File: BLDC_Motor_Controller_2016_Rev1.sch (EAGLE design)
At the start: 103 parts, among them J3 APP_2POS_CONFIG5V_HORIZ, Q1 MOSFET-NCHANNELFQP30N06L, Q2 MOSFET-NCHANNELFQP30N06L, Q3 MOSFET-NCHANNELFQP30N06L, Q4 MOSFET-NCHANNELFQP30N06L, Q5 MOSFET-NCHANNELFQP30N06L, Q6 MOSFET-NCHANNELFQP30N06L, Q7 MOSFET-PCHANNEL, Q8 MOSFET-PCHANNEL

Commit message: Fixed first board review issues
- FET for PVDD LED
- Widened input voltage polygon
- Added 15V zener on FET gates
- Added test points
- Added pull ups on hall-effect lines
- Added filter on PWM input
- Changed voltage divider resistor values
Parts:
- added 1M, 3M: 330, SparkFun-Passives:RESISTOR0805-RES
- added C40: .015u, SparkFun-Passives:CAP0805
- added D10, D11, D12, D13, D14, D15: 3.3V, SparkFun-DiscreteSemi:DIODE-ZENER3.3V
- added Q9: MOSFET-NCHANNELAO3404A, SparkFun-DiscreteSemi:MOSFET-NCHANNELAO3404A
- added R31: 100, SparkFun-Passives:RESISTOR0805-RES
- added R36, R37, R38: 10k, SparkFun-Passives:RESISTOR0805-RES
- added U$10, U$11, U$12, U$15, U$16, U$17, U$18, U$19, U$20, U$21, U$22, U$23, U$24, U$25: TEST_POINT_0.1INDIAM, MRDT-Connectors:TEST_POINT_0.1INDIAM
- R14, R19, R24, R26: value 34.8k -> 46.4k
- R32: value 1k -> 330; device SparkFun-Passives:RESISTOR1206 -> SparkFun-Passives:RESISTOR0805-RES
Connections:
- new net N$37: R31.2, U$4.4
- new net N$38: 1M.1, 3M.2, Q9.G
- new net N$41: D6.A, Q9.S
- new net N$42: U$20.P$1
- new net N$43: U$21.P$1
- new net N$44: U$22.P$1
- new net N$45: U$23.P$1
- new net N$46: U$24.P$1
- new net N$47: U$25.P$1
- net GH_A: now also U$17.P$1
- net GH_B: now also U$19.P$1
- net GL_A: now also U$18.P$1
- net GND: now also 1M.2, C40.2, D15.A
- net N$13: now also D13.C
- net N$14: now also D11.C
- net N$15: now also D10.C
- net N$16: now also D12.C
- net N$17: now also D14.C
- net N$18: now also D15.C
- net N$20: now also R36.2
- net N$33: now also R38.2
- net N$39: now also R37.2
- net PVDD: now also 3M.1, U$10.P$1; no longer D6.A
- net SH_A: now also D13.A, U$12.P$1
- net SH_B: now also D11.A, U$15.P$1
- net SH_C: now also D14.A, U$16.P$1
- net SL_A: now also D12.A
- net SL_B: now also D10.A
- net SPEED_IN: now also C40.1, R31.1; no longer U$4.4
- net VCC: now also Q9.D, R36.1, R37.1, R38.1, U$11.P$1
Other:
- moved on the sheet: D6, R32

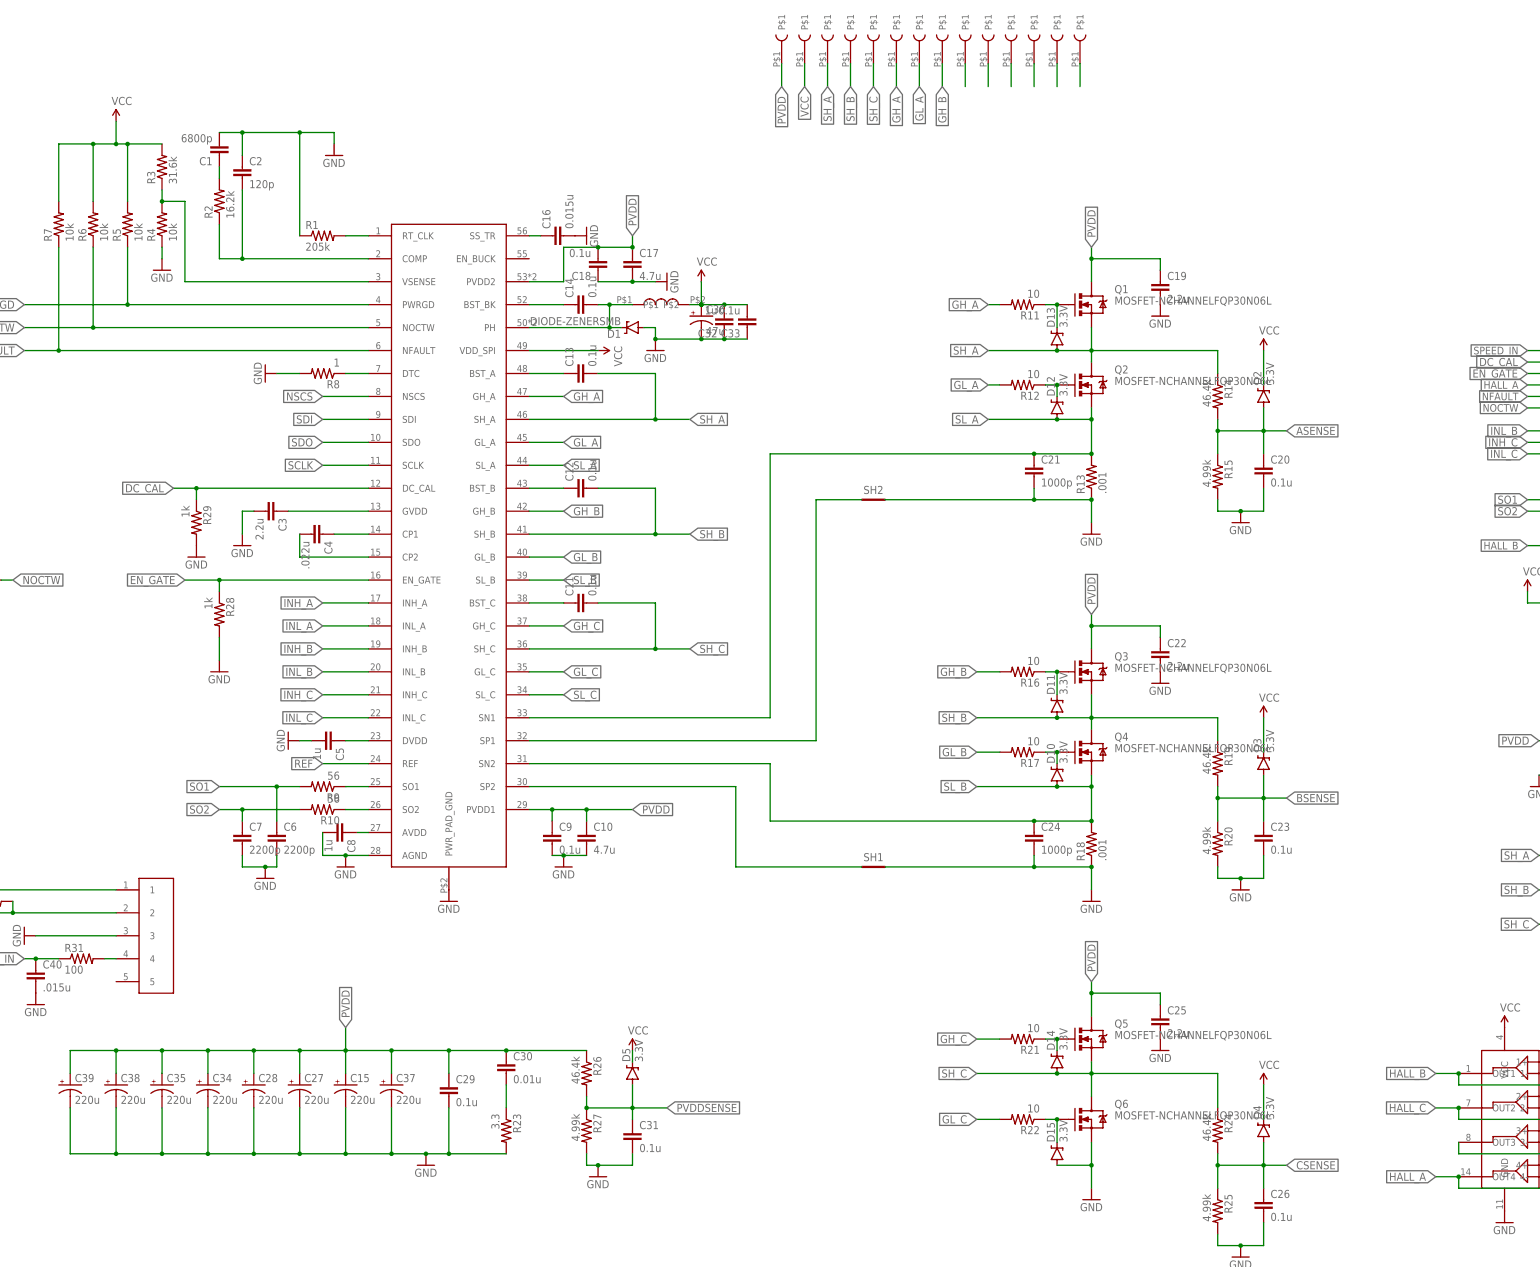
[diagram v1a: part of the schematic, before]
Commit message: Routed test points
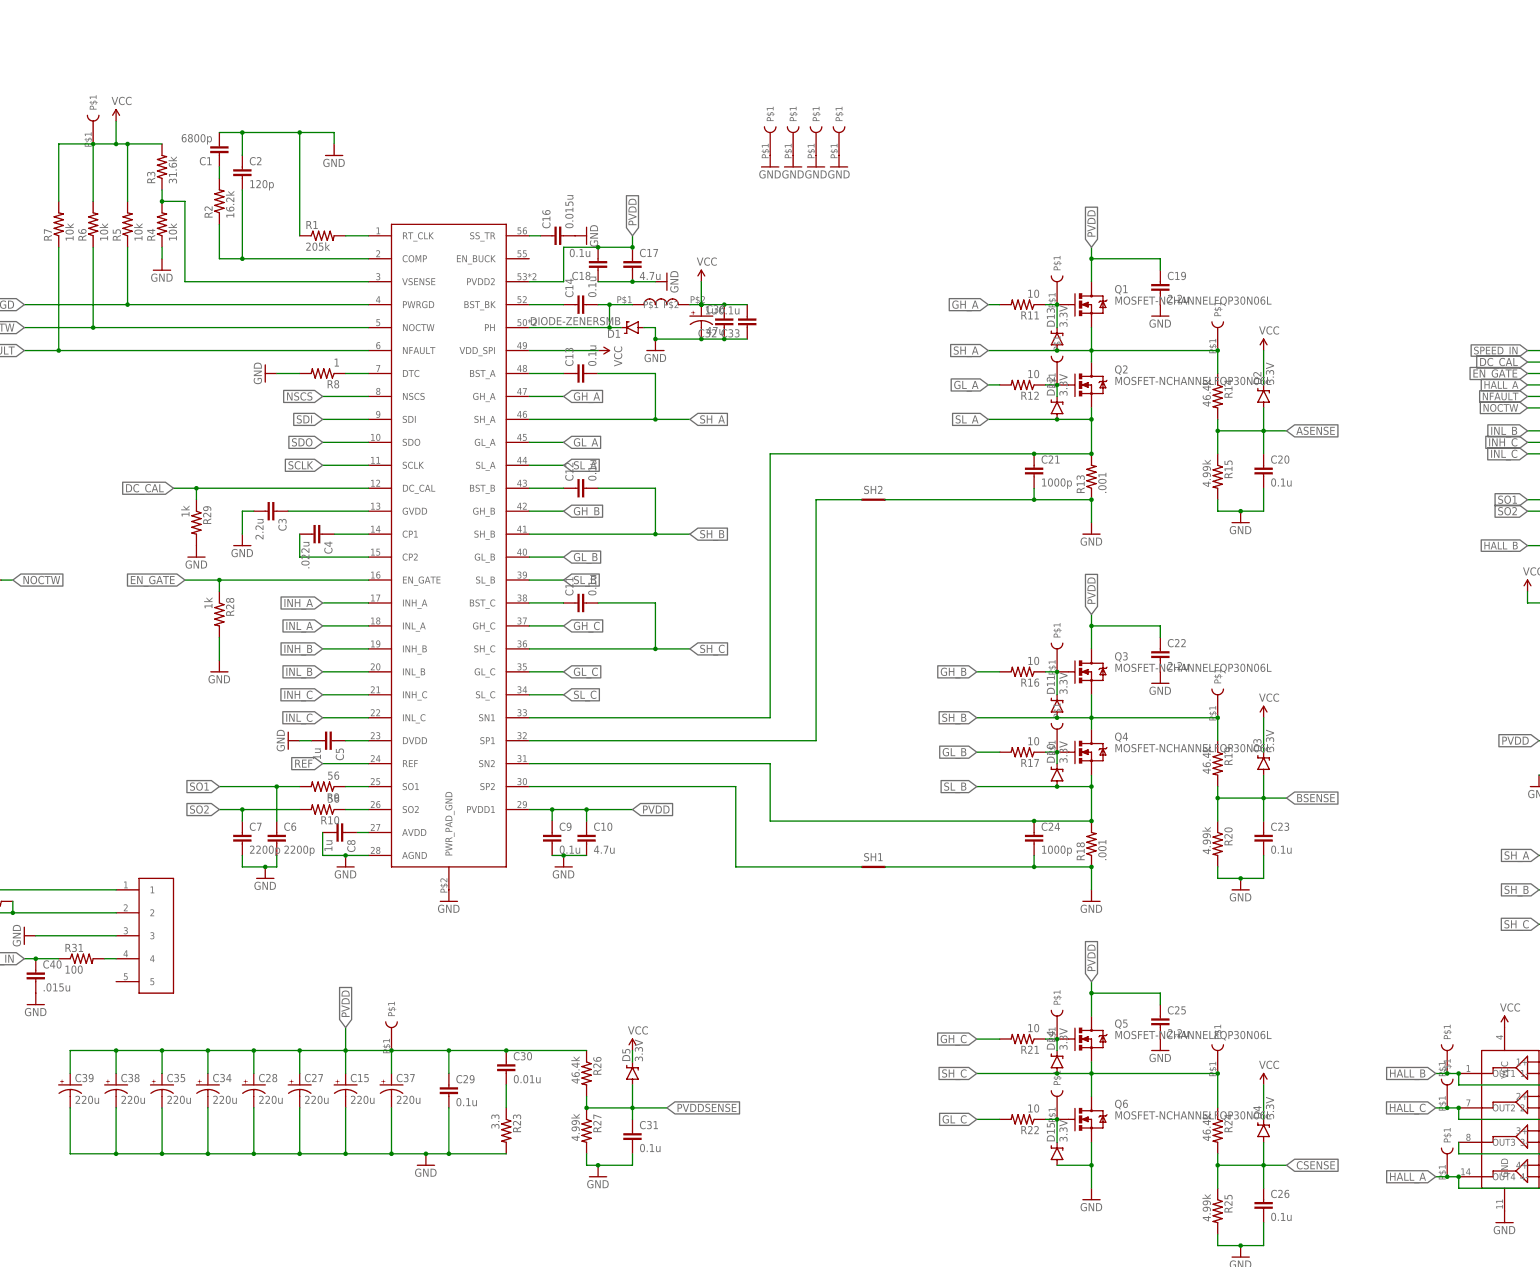
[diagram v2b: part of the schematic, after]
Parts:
- added U$26, U$27, U$28, U$29: TEST_POINT_0.1INDIAM, MRDT-Connectors:TEST_POINT_0.1INDIAM
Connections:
- removed net N$42: U$20.P$1
- removed net N$43: U$21.P$1
- removed net N$44: U$22.P$1
- removed net N$45: U$23.P$1
- removed net N$46: U$24.P$1
- removed net N$47: U$25.P$1
- net GH_A: no longer U$17.P$1
- net GH_B: no longer U$19.P$1
- net GL_A: no longer U$18.P$1
- net GND: now also U$26.P$1, U$27.P$1, U$28.P$1, U$29.P$1
- net HALL_A: now also U$23.P$1
- net HALL_B: now also U$21.P$1
- net HALL_C: now also U$22.P$1
- net N$13: now also U$12.P$1
- net N$14: now also U$16.P$1
- net N$15: now also U$17.P$1
- net N$16: now also U$15.P$1
- net N$17: now also U$18.P$1
- net N$18: now also U$19.P$1
- net PVDD: now also U$11.P$1; no longer U$10.P$1
- net SH_A: now also U$25.P$1; no longer U$12.P$1
- net SH_B: now also U$24.P$1; no longer U$15.P$1
- net SH_C: now also U$20.P$1; no longer U$16.P$1
- net VCC: now also U$10.P$1; no longer U$11.P$1

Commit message: Fixed board review #2 issues
- Increased polygon isolation
- Removed hall effect buffer and added RC filters on hall effect lines
- Added ground vias around driver backplate
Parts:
- removed U$13: OPAMP_14SOIC, OpAmp_14SOIC:OPAMP_14SOIC
- added C41, C42, C43: .015u, SparkFun-Passives:CAP0805
- added D16: 3.3V, SparkFun-DiscreteSemi:DIODE-ZENER3.3V
- added R39, R40, R41: 10, SparkFun-Passives:RESISTOR0805-RES
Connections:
- removed net N$40: U$13.3-, U$13.OUT3
- net GND: now also C41.2, C42.2, C43.2; no longer U$13.GND
- net HALL_A: now also C41.1, R41.1, U$22.P$1; no longer U$13.4-, U$13.OUT4, U$23.P$1
- net HALL_B: now also C42.1, R40.1; no longer U$13.1-, U$13.OUT1
- net HALL_C: now also C43.1, R39.1, U$23.P$1; no longer U$13.2-, U$13.OUT2, U$22.P$1
- net N$20: now also R37.2, R39.2, U$8.2; no longer R36.2, U$13.1+, U$8.3
- net N$33: now also R36.2, R40.2, U$8.3; no longer R38.2, U$13.4+, U$8.4
- net N$38: now also D16.C
- net N$39: now also R38.2, R41.2, U$8.4; no longer R37.2, U$13.2+, U$8.2
- net N$41: now also D16.A
- net VCC: no longer U$13.VCC
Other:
- moved on the sheet: 1M, R36, R37, R38

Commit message: MAX3077 was back on board for some reason, reswitched to MAX7078
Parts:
- removed U$3: MAX3077, MRDT-2015-General:MAX3077
- added U$13: MAX3078E, MRDT-ICs:MAX3078E
- R50: value 330 -> 3M
- R51: value 330 -> 1M
- renumbered 1M to R51, 3M to R50
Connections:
- new net DE: U$13.DE, U$2.PC7
- new net NRE: U$13.NRE, U$2.PD6
- net GND: now also U$13.GND; no longer U$3.GND
- net N$34: now also U$13.A; no longer U$3.B, U$3.Z
- net N$36: now also U$13.B; no longer U$3.A, U$3.Y
- net RX: now also U$13.RO; no longer U$3.RO
- net TX: now also U$13.DI; no longer U$3.DI
- net VCC: now also U$13.VCC; no longer U$3.VCC
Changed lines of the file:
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@@
 <?xml version="1.0" encoding="utf-8"?>
 <!DOCTYPE eagle SYSTEM "eagle.dtd">
-<eagle version="7.3.0">
+<eagle version="7.4.0">
 <drawing>
 <settings>
@@
 <part name="J3" library="MRDT-Connectors" deviceset="APP_2POS_CONFIG" device="5V_HORIZ"/>
 <part name="C38" library="SparkFun-Passives" deviceset="CAP_POL" device="PTH4" value="220u"/>
-<part name="U$3" library="MRDT-2015-General" deviceset="MAX3077" device=""/>
 <part name="R30" library="SparkFun-Passives" deviceset="RESISTOR" device="0805-RES" value="120"/>
 <part name="U$4" library="Molex-SL" deviceset="5PIN" device=""/>
@@
 <part name="R38" library="SparkFun-Passives" deviceset="RESISTOR" device="0805-RES" value="10k"/>
 <part name="Q9" library="SparkFun-DiscreteSemi" deviceset="MOSFET-NCHANNEL" device="AO3404A"/>
-<part name="1M" library="SparkFun-Passives" deviceset="RESISTOR" device="0805-RES" value="330"/>
-<part name="3M" library="SparkFun-Passives" deviceset="RESISTOR" device="0805-RES" value="330"/>
+<part name="R51" library="SparkFun-Passives" deviceset="RESISTOR" device="0805-RES" value="1M"/>
+<part name="R50" library="SparkFun-Passives" deviceset="RESISTOR" device="0805-RES" value="3M"/>
 <part name="GND35" library="SparkFun-Aesthetics" deviceset="GND" device=""/>
 <part name="D10" library="SparkFun-DiscreteSemi" deviceset="DIODE-ZENER" device="3.3V" value="3.3V"/>
@@
 <part name="GND33" library="SparkFun-Aesthetics" deviceset="GND" device=""/>
 <part name="D16" library="SparkFun-DiscreteSemi" deviceset="DIODE-ZENER" device="3.3V" value="3.3V"/>
+<part name="U$13" library="MRDT-ICs" deviceset="MAX3078E" device=""/>
 </parts>
 <sheets>
@@
 <instance part="J3" gate="VCC" x="256.54" y="-45.72"/>
 <instance part="C38" gate="G$1" x="-73.66" y="-121.92"/>
-<instance part="U$3" gate="G$1" x="-121.92" y="-96.52"/>
 <instance part="R30" gate="G$1" x="-101.6" y="-81.28"/>
 <instance part="U$4" gate="G$1" x="-66.04" y="-91.44"/>
 <instance part="GND36" gate="1" x="-93.98" y="-88.9" rot="R270"/>
-<instance part="GND37" gate="1" x="-147.32" y="-101.6"/>
+<instance part="GND37" gate="1" x="-116.84" y="-93.98"/>
 <instance part="C39" gate="G$1" x="-83.82" y="-121.92"/>
 <instance part="SH1" gate="G$1" x="93.98" y="-73.66"/>
@@
 <instance part="R38" gate="G$1" x="261.62" y="-116.84" rot="R270"/>
 <instance part="Q9" gate="G$1" x="-165.1" y="-12.7"/>
-<instance part="1M" gate="G$1" x="-177.8" y="-20.32" rot="R270"/>
-<instance part="3M" gate="G$1" x="-182.88" y="-12.7"/>
+<instance part="R51" gate="G$1" x="-177.8" y="-20.32" rot="R270"/>
+<instance part="R50" gate="G$1" x="-182.88" y="-12.7"/>
 <instance part="GND35" gate="1" x="-177.8" y="-30.48"/>
 <instance part="D10" gate="G$1" x="134.62" y="-53.34" rot="R90"/>
@@
 <instance part="GND33" gate="1" x="241.3" y="-154.94"/>
 <instance part="D16" gate="G$1" x="-172.72" y="-17.78" rot="R90"/>
+<instance part="U$13" gate="G$1" x="-127" y="-81.28"/>
 </instances>
 <busses>
@@
 </segment>
 <segment>
-<pinref part="U$3" gate="G$1" pin="GND"/>
-<pinref part="GND37" gate="1" pin="GND"/>
-<wire x1="-144.78" y1="-93.98" x2="-147.32" y2="-93.98" width="0.1524" layer="91"/>
-<wire x1="-147.32" y1="-93.98" x2="-147.32" y2="-99.06" width="0.1524" layer="91"/>
-</segment>
-<segment>
 <pinref part="U$4" gate="G$1" pin="3"/>
 <pinref part="GND36" gate="1" pin="GND"/>
@@
 </segment>
 <segment>
-<pinref part="1M" gate="G$1" pin="2"/>
+<pinref part="R51" gate="G$1" pin="2"/>
 <pinref part="GND35" gate="1" pin="GND"/>
 <wire x1="-177.8" y1="-27.94" x2="-177.8" y2="-25.4" width="0.1524" layer="91"/>
@@
 <pinref part="C42" gate="G$1" pin="2"/>
 <wire x1="241.3" y1="-149.86" x2="241.3" y2="-152.4" width="0.1524" layer="91"/>
+</segment>
+<segment>
+<pinref part="U$13" gate="G$1" pin="GND"/>
+<pinref part="GND37" gate="1" pin="GND"/>
+<wire x1="-116.84" y1="-91.44" x2="-116.84" y2="-88.9" width="0.1524" layer="91"/>
 </segment>
 </net>
@@
 </segment>
 <segment>
-<pinref part="U$3" gate="G$1" pin="VCC"/>
-<wire x1="-144.78" y1="-78.74" x2="-147.32" y2="-78.74" width="0.1524" layer="91"/>
-<wire x1="-147.32" y1="-78.74" x2="-147.32" y2="-73.66" width="0.1524" layer="91"/>
-<label x="-147.32" y="-73.66" size="1.778" layer="95" rot="R90" xref="yes"/>
+<wire x1="-116.84" y1="-73.66" x2="-116.84" y2="-71.12" width="0.1524" layer="91"/>
+<label x="-116.84" y="-71.12" size="1.778" layer="95" rot="R90" xref="yes"/>
+<pinref part="U$13" gate="G$1" pin="VCC"/>
 </segment>
 <segment>
@@
 </segment>
 <segment>
-<pinref part="3M" gate="G$1" pin="1"/>
+<pinref part="R50" gate="G$1" pin="1"/>
 <wire x1="-187.96" y1="-5.08" x2="-187.96" y2="-12.7" width="0.1524" layer="91"/>
 <label x="-187.96" y="-5.08" size="1.778" layer="95" rot="R90" xref="yes"/>
@@
 </segment>
 <segment>
-<pinref part="U$3" gate="G$1" pin="DI"/>
-<wire x1="-144.78" y1="-88.9" x2="-147.32" y2="-88.9" width="0.1524" layer="91"/>
-<label x="-147.32" y="-88.9" size="1.778" layer="95" rot="R180" xref="yes"/>
+<wire x1="-139.7" y1="-88.9" x2="-144.78" y2="-88.9" width="0.1524" layer="91"/>
+<label x="-144.78" y="-88.9" size="1.778" layer="95" rot="R180" xref="yes"/>
+<pinref part="U$13" gate="G$1" pin="DI"/>
 </segment>
 </net>
@@
 </segment>
 <segment>
-<pinref part="U$3" gate="G$1" pin="RO"/>
-<wire x1="-144.78" y1="-83.82" x2="-147.32" y2="-83.82" width="0.1524" layer="91"/>
-<label x="-147.32" y="-83.82" size="1.778" layer="95" rot="R180" xref="yes"/>
+<wire x1="-139.7" y1="-73.66" x2="-144.78" y2="-73.66" width="0.1524" layer="91"/>
+<label x="-144.78" y="-73.66" size="1.778" layer="95" rot="R180" xref="yes"/>
+<pinref part="U$13" gate="G$1" pin="RO"/>
 </segment>
 </net>
@@
 <net name="N$34" class="0">
 <segment>
-<pinref part="U$3" gate="G$1" pin="B"/>
-<pinref part="U$3" gate="G$1" pin="Z"/>
-<wire x1="-116.84" y1="-83.82" x2="-116.84" y2="-88.9" width="0.1524" layer="91"/>
 <pinref part="U$4" gate="G$1" pin="2"/>
 <wire x1="-116.84" y1="-83.82" x2="-96.52" y2="-83.82" width="0.1524" layer="91"/>
-<junction x="-116.84" y="-83.82"/>
 <pinref part="R30" gate="G$1" pin="2"/>
 <wire x1="-96.52" y1="-83.82" x2="-73.66" y2="-83.82" width="0.1524" layer="91"/>
 <wire x1="-96.52" y1="-81.28" x2="-96.52" y2="-83.82" width="0.1524" layer="91"/>
 <junction x="-96.52" y="-83.82"/>
+<pinref part="U$13" gate="G$1" pin="A"/>
 </segment>
 </net>
 <net name="N$36" class="0">
 <segment>
-<pinref part="U$3" gate="G$1" pin="A"/>
-<wire x1="-116.84" y1="-78.74" x2="-114.3" y2="-78.74" width="0.1524" layer="91"/>
-<wire x1="-114.3" y1="-78.74" x2="-114.3" y2="-93.98" width="0.1524" layer="91"/>
-<pinref part="U$3" gate="G$1" pin="Y"/>
-<wire x1="-114.3" y1="-93.98" x2="-116.84" y2="-93.98" width="0.1524" layer="91"/>
 <pinref part="U$4" gate="G$1" pin="1"/>
-<wire x1="-114.3" y1="-78.74" x2="-106.68" y2="-78.74" width="0.1524" layer="91"/>
-<junction x="-114.3" y="-78.74"/>
+<wire x1="-116.84" y1="-78.74" x2="-106.68" y2="-78.74" width="0.1524" layer="91"/>
 <pinref part="R30" gate="G$1" pin="1"/>
 <wire x1="-106.68" y1="-78.74" x2="-73.66" y2="-78.74" width="0.1524" layer="91"/>
 <wire x1="-106.68" y1="-81.28" x2="-106.68" y2="-78.74" width="0.1524" layer="91"/>
 <junction x="-106.68" y="-78.74"/>
+<pinref part="U$13" gate="G$1" pin="B"/>
 </segment>
 </net>
@@
 <segment>
 <pinref part="Q9" gate="G$1" pin="G"/>
-<pinref part="3M" gate="G$1" pin="2"/>
+<pinref part="R50" gate="G$1" pin="2"/>
 <wire x1="-172.72" y1="-12.7" x2="-177.8" y2="-12.7" width="0.1524" layer="91"/>
-<pinref part="1M" gate="G$1" pin="1"/>
+<pinref part="R51" gate="G$1" pin="1"/>
 <wire x1="-177.8" y1="-15.24" x2="-177.8" y2="-12.7" width="0.1524" layer="91"/>
 <junction x="-177.8" y="-12.7"/>
@@
 </segment>
 </net>
+<net name="NRE" class="0">
+<segment>
+<pinref part="U$13" gate="G$1" pin="NRE"/>
+<wire x1="-139.7" y1="-78.74" x2="-144.78" y2="-78.74" width="0.1524" layer="91"/>
+<label x="-144.78" y="-78.74" size="1.778" layer="95" rot="R180" xref="yes"/>
+</segment>
+<segment>
+<pinref part="U$2" gate="G$1" pin="PD6"/>
+<wire x1="276.86" y1="7.62" x2="284.48" y2="7.62" width="0.1524" layer="91"/>
+<label x="284.48" y="7.62" size="1.778" layer="95" xref="yes"/>
+</segment>
+</net>
+<net name="DE" class="0">
+<segment>
+<pinref part="U$13" gate="G$1" pin="DE"/>
+<wire x1="-139.7" y1="-83.82" x2="-144.78" y2="-83.82" width="0.1524" layer="91"/>
+<label x="-144.78" y="-83.82" size="1.778" layer="95" rot="R180" xref="yes"/>
+</segment>
+<segment>
+<pinref part="U$2" gate="G$1" pin="PC7"/>
+<wire x1="246.38" y1="15.24" x2="238.76" y2="15.24" width="0.1524" layer="91"/>
+<label x="238.76" y="15.24" size="1.778" layer="95" rot="R180" xref="yes"/>
+</segment>
+</net>

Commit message: Changed net flag sizes, rerouted some things
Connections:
- net SPEED_IN renamed PWM_IN
- net N$37: now also U$4.5; no longer U$4.4
- net NRE: now also U$13.!RE; no longer U$13.NRE
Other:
- moved on the sheet: C40, R31
